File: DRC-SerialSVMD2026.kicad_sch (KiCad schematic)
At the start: 35 parts, among them J1 CAN, J10 BATT, J11 SerialServo1, J12 SerialServo2, J13 SerialServo3, J14 SerialServo4, J2 CAN, J3 STLINK, J4 SW1, J5 SW2, J6 SW3, J7 SW4, J8 SW5, J9 SW6, SW1 DIP, U1 RT9080-33GJ5, U6 BP5293-50

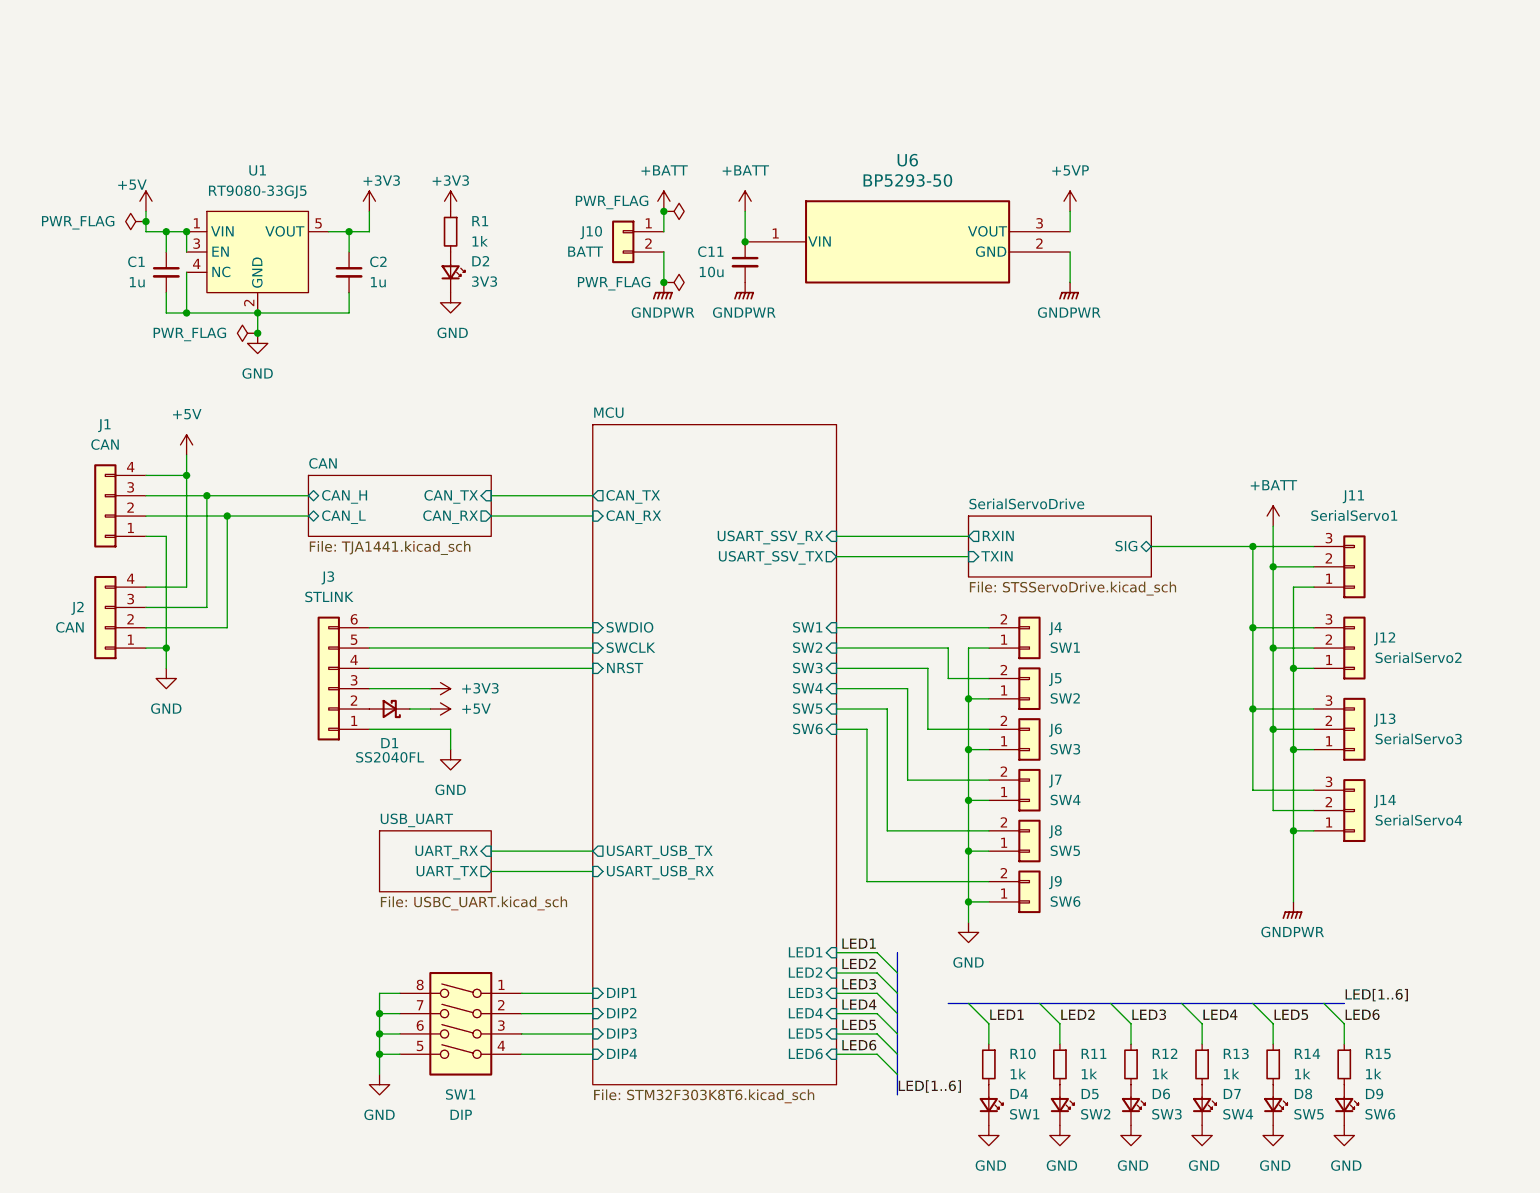
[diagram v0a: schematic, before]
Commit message: サーボと直接シリアル通信するためのUSB端子を追加、v0.1.1
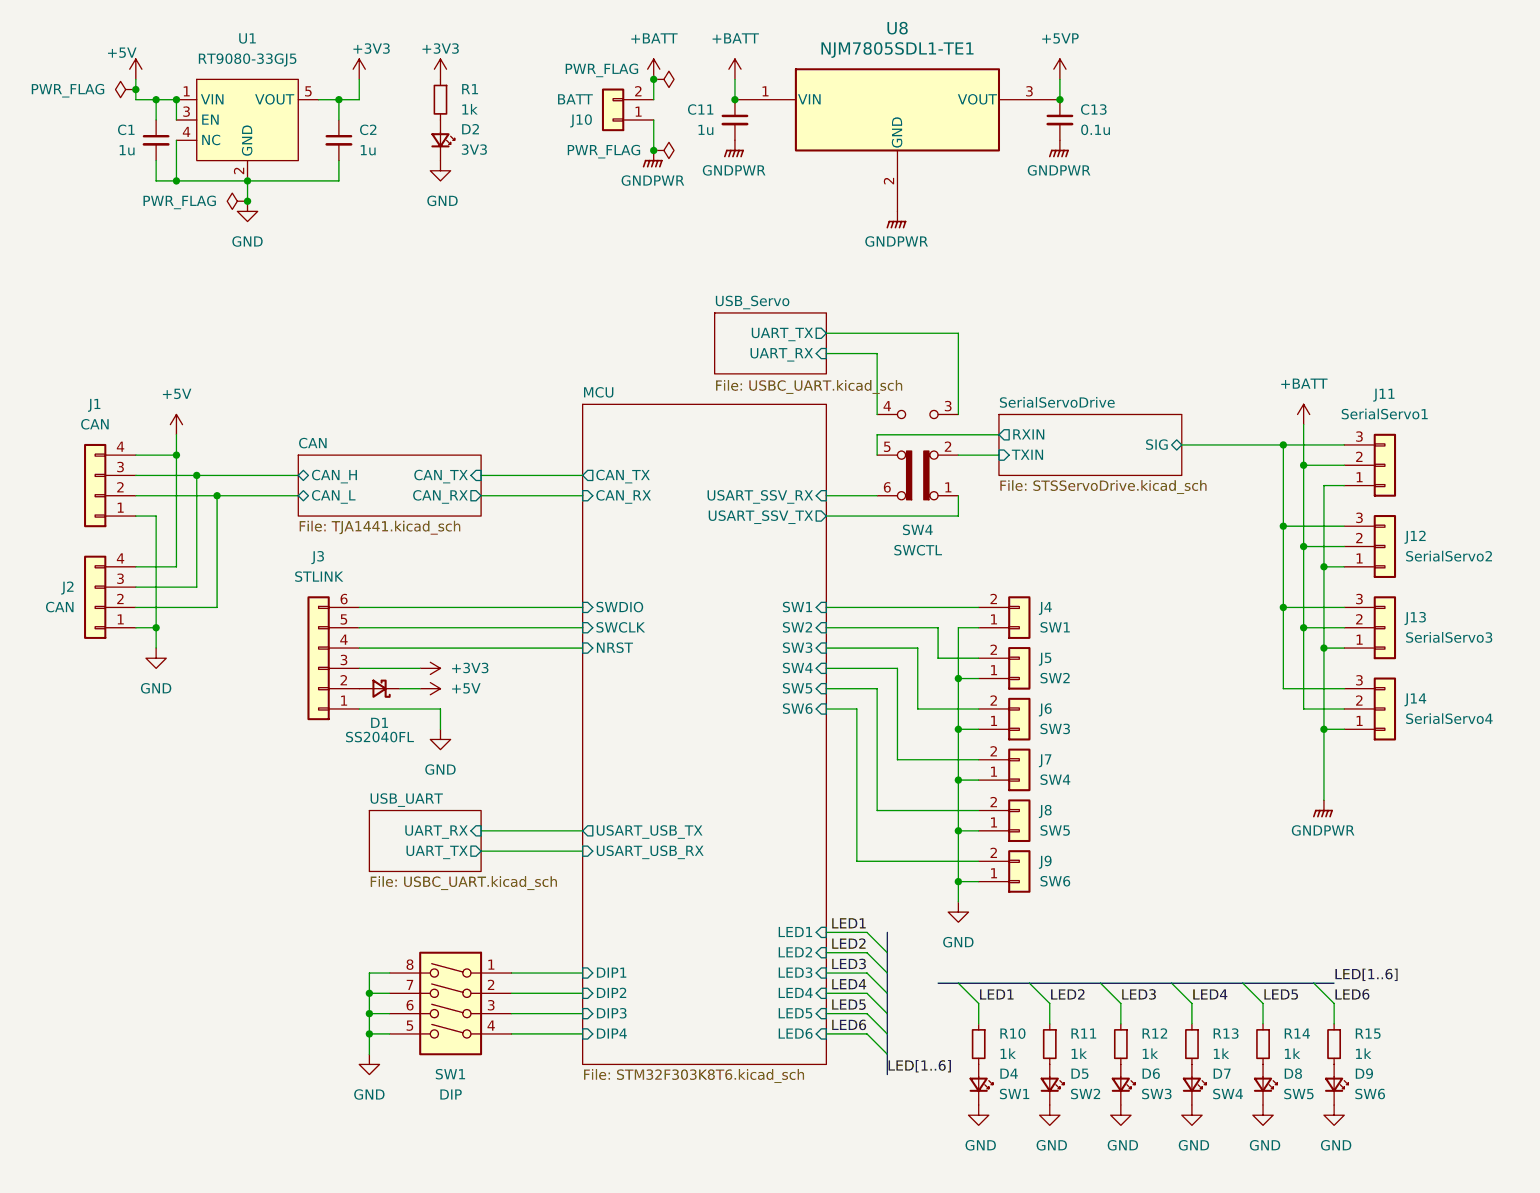
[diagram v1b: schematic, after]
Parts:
- removed U6: BP5293-50, lib:SIP03_BP5293_17X7P2_ROM, symbol lib:BP5293-50
- added C13: 0.1u, Capacitor_SMD:C_0603_1608Metric_Pad1.08x0.95mm_HandSolder, symbol Device:C_Small
- added SW4: SWCTL, lib:IS-2235, symbol Switch:SW_Slide_DPDT
- added U8: NJM7805SDL1-TE1, lib:TO-252-3-L1_NMD, symbol lib:NJM7805SDL1-TE1
- C1, C2: footprint Capacitor_SMD:C_0805_2012Metric_Pad1.18x1.45mm_HandSolder -> Capacitor_SMD:C_0603_1608Metric_Pad1.08x0.95mm_HandSolder
- C11: value 10u -> 1u; footprint Capacitor_SMD:C_0805_2012Metric_Pad1.18x1.45mm_HandSolder -> Capacitor_SMD:C_0603_1608Metric_Pad1.08x0.95mm_HandSolder
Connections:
- net +5VP: now also C13.1, U8.3 (VOUT)
- net +BATT: now also J10.2 (Pin_2), U8.1 (VIN); no longer J10.1 (Pin_1)
- net GNDPWR: now also J10.1 (Pin_1), C13.2, U8.2 (GND); no longer J10.2 (Pin_2)
- net MCU/USART_SSV_RX: now also SW4.6 (C)
- net MCU/USART_SSV_TX: now also SW4.1 (A)
- new net SerialServoDrive/RXIN: SW4.5 (B)
- new net SerialServoDrive/TXIN: SW4.2 (B)
- new net USB_Servo/UART_RX: SW4.4 (A)
- new net USB_Servo/UART_TX: SW4.3 (C)
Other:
- added sheet USB_Servo (USBC_UART.kicad_sch)
- moved on the sheet: C1, C11, C2, D1, D2, D4, D5, D6, D7, D8, D9, J1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
